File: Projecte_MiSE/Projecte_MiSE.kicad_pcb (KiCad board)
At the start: 2 copper layers, 80 x 75 mm, 36 parts, among them IC1 MSP430FR2355TPT, J1 C_DFrobot, J2 Conn_01x03_Pin, J3 ESP01, J4 URM10, SW1 SW_Push, U1 LMV324, Y1 Crystal_GND3

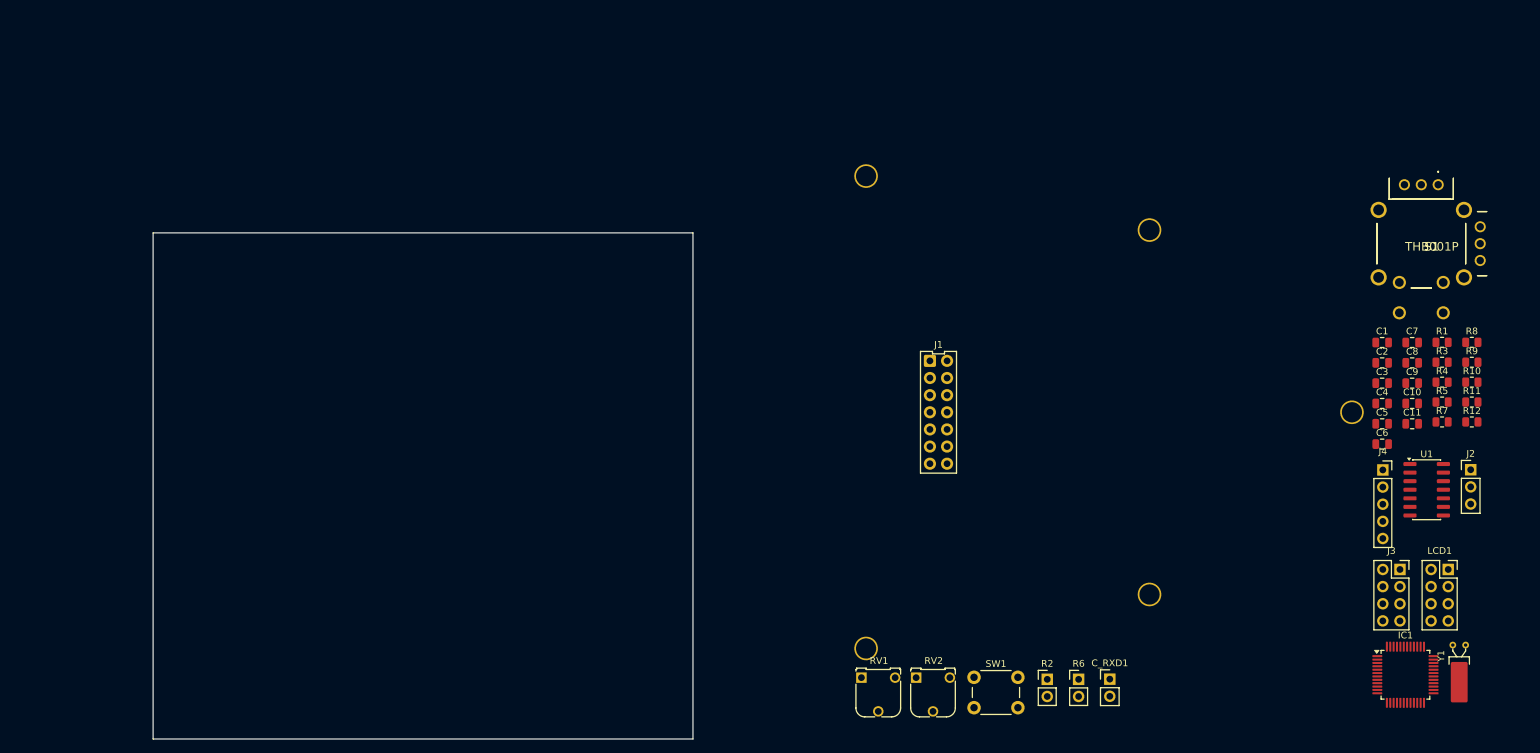
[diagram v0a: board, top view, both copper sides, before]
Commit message: layout LCD i DFrobot
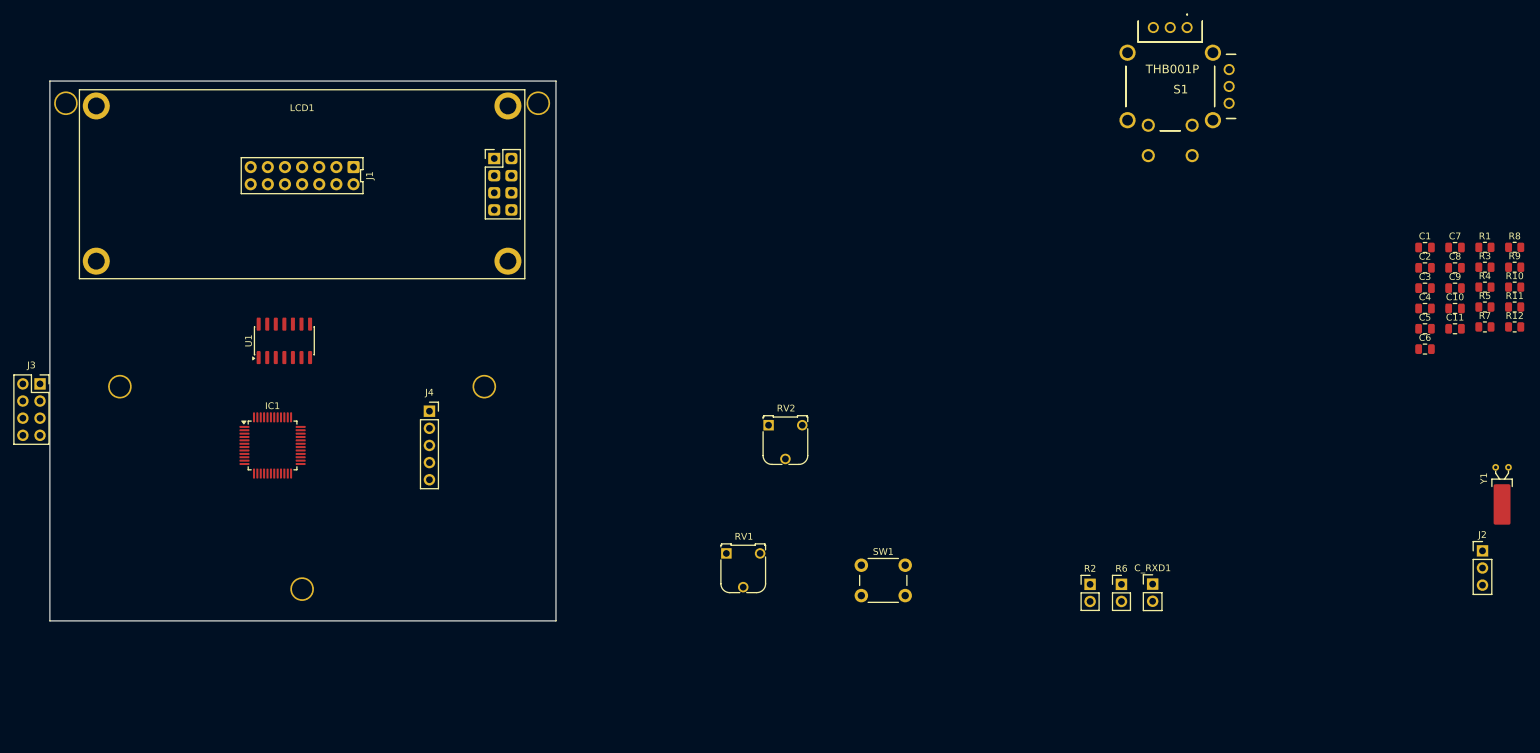
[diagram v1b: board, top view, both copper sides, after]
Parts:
- LCD1: footprint Connector_PinSocket_2.54mm:PinSocket_2x04_P2.54mm_Vertical -> MiSE:LCD_2x16_I2C(Midas)
- moved J3 203.4 mm to (28.8, 77.4)
- moved LCD1 179.2 mm to (67.6, 47.8)
- moved IC1 171.3 mm to (63.2, 86.5)
- moved U1 170.7 mm to (65.0, 71.0), turned to 90 degrees
- moved J4 141.5 mm to (86.5, 81.4)
- moved J1 101.4 mm to (67.6, 47.8), turned to -90 degrees
- moved S1 43.9 mm to (198.8, 24.6)
- moved RV2 43.3 mm to (136.8, 83.5)
- moved RV1 27.2 mm to (130.5, 102.5)
- moved Y1 27.1 mm to (244.5, 89.8)
- moved SW1 23.6 mm to (150.5, 104.2)
- moved C11 15.4 mm to (238.5, 69.2)
- moved C5 15.4 mm to (234.0, 69.2)
- moved R6 15.4 mm to (189.1, 107.1)
- moved C2 15.4 mm to (234.0, 60.2)
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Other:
- board size 80 x 75 mm -> 75 x 80 mm

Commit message: footprints and layout
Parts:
- removed C_RXD1: C_TXD, Connector_PinHeader_2.54mm:PinHeader_1x02_P2.54mm_Vertical
- added D1: LED, LED_SMD:LED_0805_2012Metric, F.Cu at (56.5, 80.2)
- added J10: Conn_GND_TP, Connector_PinHeader_1.00mm:PinHeader_1x01_P1.00mm_Vertical, F.Cu at (73.2, 107.0)
- added J11: Conn_TXD_TP, Connector_PinHeader_1.00mm:PinHeader_1x01_P1.00mm_Vertical, F.Cu at (90.5, 75.2)
- added J12: Conn_RXD_TP, Connector_PinHeader_1.00mm:PinHeader_1x01_P1.00mm_Vertical, F.Cu at (90.5, 69.8)
- added J5: Conn_GND_TP, Connector_PinHeader_1.00mm:PinHeader_1x01_P1.00mm_Vertical, F.Cu at (60.0, 107.0)
- added J6: Conn_ACLK_TP, Connector_PinHeader_1.00mm:PinHeader_1x01_P1.00mm_Vertical, F.Cu at (79.5, 91.5)
- added J7: Conn_SMCLK_TP, Connector_PinHeader_1.00mm:PinHeader_1x01_P1.00mm_Vertical, F.Cu at (79.5, 88.0)
- added J8: Conn_SDA_TP, Connector_PinHeader_1.00mm:PinHeader_1x01_P1.00mm_Vertical, F.Cu at (103.5, 51.5)
- added J9: Conn_SCL_TP, Connector_PinHeader_1.00mm:PinHeader_1x01_P1.00mm_Vertical, F.Cu at (103.5, 43.8)
- added R13: R, Resistor_SMD:R_0805_2012Metric, F.Cu at (53.0, 80.2)
- C1, C2: value C -> 15p
- C3: value C -> 1n
- C4, C5, C6, C7, C8, C9: value C -> 100n
- J2: value Conn_01x03_Pin -> Conn_SWB
- J3: value ESP01 -> ESP01_WIFI
- R3: value R -> 47k
- R4, R5: value R -> 2k2
- R7: value R -> 10k
- SW1: value SW_Push -> ~{RST}
- moved C11 205.4 mm to (33.8, 85.5), turned to 90 degrees
- moved C9 204.6 mm to (34.8, 82.2)
- moved R10 192.9 mm to (56.8, 93.1), turned to 90 degrees
- moved R12 191.2 mm to (58.1, 96.0), turned to 180 degrees
- moved R11 190.3 mm to (59.0, 93.2), turned to -90 degrees
- moved S1 178.0 mm to (33.3, 90.1), turned to 90 degrees
- moved R9 176.5 mm to (73.0, 87.5)
- moved R8 175.9 mm to (74.5, 90.3), turned to -90 degrees
- moved R7 175.0 mm to (67.9, 72.8), turned to 180 degrees
- moved R1 174.1 mm to (72.0, 90.2), turned to 90 degrees
- moved Y1 172.9 mm to (72.0, 78.2), turned to 90 degrees
- moved C10 167.4 mm to (73.2, 93.2)
- moved C2 162.5 mm to (72.0, 73.2), turned to 90 degrees
- moved C5 162.0 mm to (74.3, 42.2), turned to 180 degrees
- moved C4 160.5 mm to (74.3, 50.8), turned to 180 degrees
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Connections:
- net Net-(IC1-P2.1/TB1.2/COMP1.O) renamed /echo
- net Net-(IC1-P4.5/UCB1CLK) renamed /~{RST_{LCD}}
- net Net-(IC1-TEST/SBWTCK) renamed /SBWTCK
- net Net-(IC1-~{RST}/NMI/SBWTDIO) renamed /SBWTDIO
- net Net-(U1A-+) renamed /THR
- net Net-(U1B--) renamed /THL
- net Net-(U1C-+) renamed /THU
- net Net-(U1D--) renamed /THD
- C4 pad 1: Net-(J1-Pin_1) -> +3.3V
- C5 pad 1: Net-(J1-Pin_2) -> +3.3V
- C9 pad 1: Net-(J4-Pin_1) -> +3.3V
- IC1 pad 15: unconnected-(IC1-P4.4/UCB1STE-Pad15) -> /EN
- IC1 pad 17: /EN -> unconnected-(IC1-P6.5/TB3.6-Pad17)
- IC1 pad 2: unconnected-(IC1-P1.1/UCB0CLK/ACLK/OA0O/COMP0.1/A1-Pad2) -> /ACLK_TP
- IC1 pad 3: unconnected-(IC1-P1.0/UCB0STE/SMCLK/COMP0.0/A0/VEREF+-Pad3) -> /SMCLK_TP
- IC1 pad 30: unconnected-(IC1-P2.0/TB1.1/COMP0.O-Pad30) -> /M_L
- J1 pad 1: Net-(J1-Pin_1) -> +3.3V
- J1 pad 2: Net-(J1-Pin_2) -> +3.3V
- J4 pad 1: Net-(J4-Pin_1) -> +3.3V
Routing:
- added copper zone on F.Cu, net +3.3V
- added copper zone on B.Cu, net GND

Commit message: layout and schem pins
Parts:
- moved J11 10.2 mm to (100.2, 78.2)
- moved C8 7.20 mm to (102.0, 63.8), turned to 0 degrees
- moved C5 2.50 mm to (76.8, 42.8), turned to 0 degrees
- moved C4 2.01 mm to (76.2, 50.2), turned to 0 degrees
- moved C6 1.40 mm to (75.7, 80.2)
- moved J6 1.25 mm to (79.5, 92.8)
- moved J7 1.25 mm to (79.5, 89.2)
- moved C2 1.01 mm to (73.0, 73.0)
- moved R11 1.00 mm to (59.0, 92.2)
- moved R12 1.00 mm to (58.1, 95.0)
- moved Y1 1.00 mm to (73.0, 78.2)
- moved R10 0.93 mm to (56.8, 92.2)
- moved R4 0.75 mm to (101.8, 46.7)
- moved R7 0.35 mm to (67.7, 73.0)
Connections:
- IC1 pad 18: /P12 -> /P0
- IC1 pad 19: /P8 -> /P1
- IC1 pad 21: /P1 -> /P8
- IC1 pad 22: /P0 -> /P12
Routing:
- net /SCL: track 0.00 -> 82.1 mm, vias 0 -> 1
- net /SDA: track 0.00 -> 79.8 mm, vias 0 -> 2
- net /TXD: track 0.00 -> 53.1 mm, vias 0 -> 4
- net /RXD: track 0.42 -> 50.9 mm, vias 0 -> 2
- net /LDRR: track 0.00 -> 46.1 mm, vias 0 -> 2
- net /LDRL: track 0.00 -> 45.5 mm, vias 0 -> 2
- net /~{RST_{LCD}}: track 0.00 -> 45.4 mm, vias 0 -> 2
- net /EN: track 0.00 -> 42.3 mm, vias 0 -> 2
- net /SBWTDIO: track 0.00 -> 32.5 mm
- net /P0: track 0.00 -> 30.6 mm
- net /P1: track 0.00 -> 29.7 mm
- net /P2: track 0.00 -> 28.9 mm
- net /trg: track 0.00 -> 28.6 mm
- net /P8: track 0.00 -> 28.0 mm
- net /P12: track 0.00 -> 28.0 mm
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
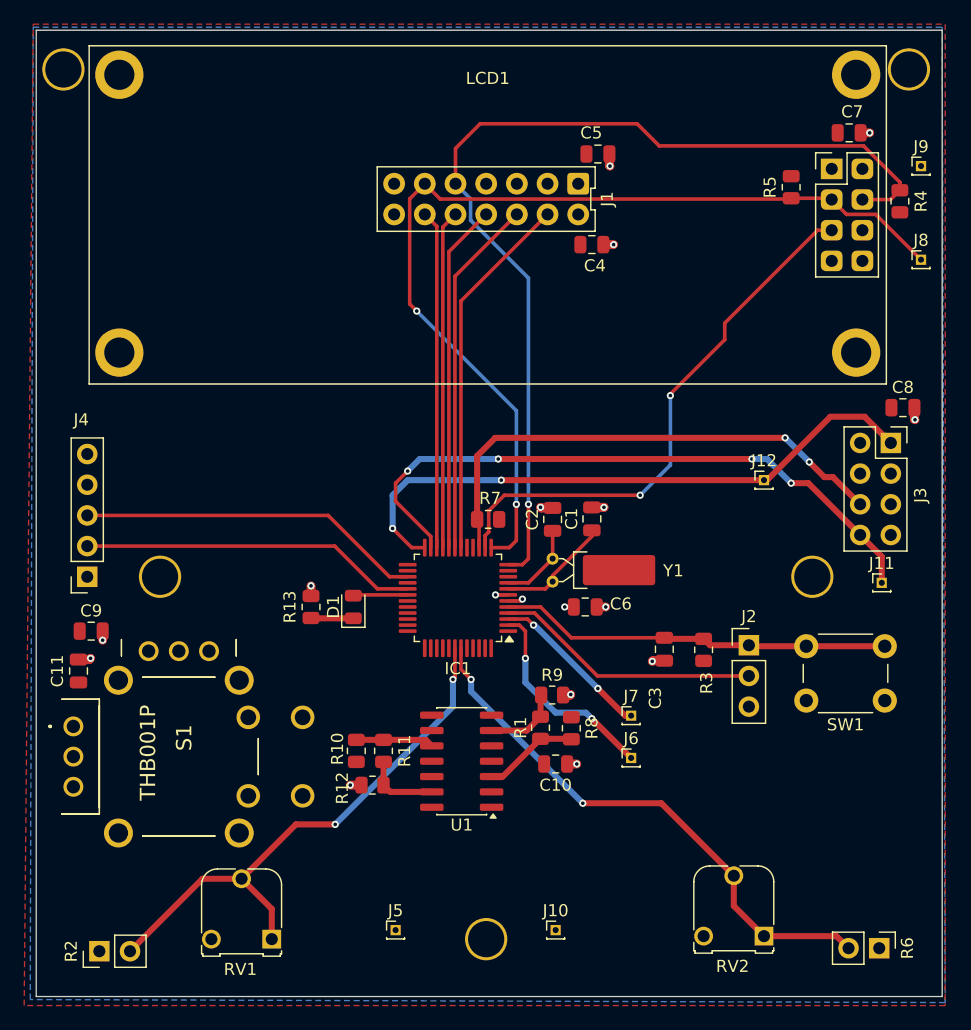
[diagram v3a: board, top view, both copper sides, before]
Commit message: component placement and routing
DRC, constrains and net classes. minor details are missing
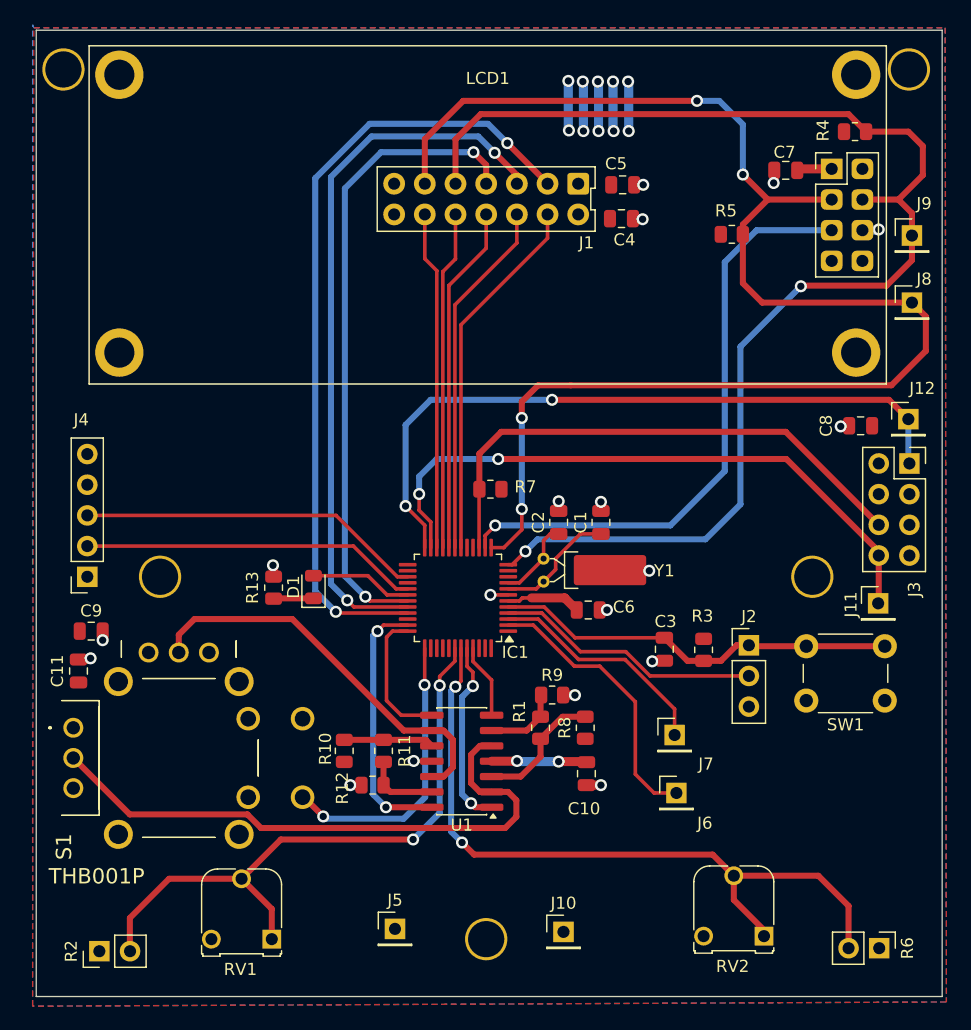
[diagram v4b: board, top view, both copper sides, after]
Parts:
- J10, J11, J12, J5, J6, J7, J8, J9: footprint Connector_PinHeader_1.00mm:PinHeader_1x01_P1.00mm_Vertical -> Connector_PinHeader_2.54mm:PinHeader_1x01_P2.54mm_Vertical
- moved J12 13.0 mm to (102.5, 64.7)
- moved R4 6.85 mm to (98.0, 40.9), turned to 0 degrees
- moved R5 6.27 mm to (87.8, 49.4), turned to 0 degrees
- moved C7 6.10 mm to (92.3, 44.1), turned to 180 degrees
- moved J9 5.80 mm to (102.8, 49.5)
- moved J6 4.74 mm to (83.2, 95.7)
- moved J7 3.94 mm to (83.1, 90.8)
- moved C8 3.81 mm to (98.5, 65.2), turned to 180 degrees
- moved D1 3.69 mm to (53.2, 78.6)
- moved J8 3.63 mm to (102.8, 55.0)
- moved R13 3.49 mm to (49.9, 78.7)
- moved C5 3.27 mm to (78.8, 45.3)
- moved C4 3.26 mm to (78.7, 48.1)
- moved C10 2.67 mm to (75.8, 94.0), turned to -90 degrees
- moved R7 2.51 mm to (67.8, 70.5)
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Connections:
- IC1 pad 35: /GPIOU -> /GPIOD
- IC1 pad 36: /GPIOD -> /GPIOU
- IC1 pad 44: /GPIOL -> /GPIOR
- IC1 pad 45: /GPIOR -> /GPIOL
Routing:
- net /SCLK: track 0.00 -> 65.8 mm, vias 0 -> 2
- net /MISO: track 0.00 -> 59.7 mm, vias 0 -> 2
- net /MOSI: track 0.00 -> 53.1 mm, vias 0 -> 2
- net /ANALOG_OUT1: track 0.00 -> 50.3 mm
- net /SDA: track 79.8 -> 120.5 mm, vias 2 -> 4
- net +3.3V: track 1.99 -> 37.6 mm, vias 2 -> 12
- net /ANALOG_OUT2: track 0.00 -> 33.2 mm
- net /SCL: track 82.1 -> 109.6 mm, vias 1 -> 2
- net /JSEL: track 0.00 -> 24.0 mm, vias 0 -> 2
- net /GPIOD: track 0.00 -> 21.7 mm, vias 0 -> 2
- net /GPIOR: track 0.00 -> 15.6 mm, vias 0 -> 2
- net /LDRL: track 45.5 -> 60.5 mm
- net /GPIOU: track 0.00 -> 11.5 mm
- net /RXD: track 50.9 -> 57.8 mm
- net GND: track 13.5 -> 20.0 mm, vias 15 -> 18
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
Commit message: Crystal
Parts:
- C1, C2: value 15p -> 12p
- R1, R10, R11, R12, R8, R9: value R -> 10k
- R13: value R -> 120
- moved C1 8.28 mm to (76.2, 81.5), turned to 0 degrees
- moved C6 8.27 mm to (70.0, 86.2), turned to -90 degrees
- moved C2 3.59 mm to (76.3, 75.5), turned to 0 degrees
- moved Y1 2.18 mm to (74.0, 79.4)
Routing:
- net /crystall-: track 10.1 -> 8.03 mm
- net +3.3V: track 37.6 -> 39.5 mm, vias 12 -> 14
- net /~{RST_{LCD}}: track 50.3 -> 49.0 mm
- net /SCL: track 109.6 -> 108.5 mm
- net /ANALOG_OUT1: track 50.3 -> 51.2 mm
- net /crystall+: track 6.73 -> 7.57 mm
- net /JSEL: track 24.0 -> 24.6 mm
- net GND: vias 18 -> 17
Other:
- board text added: "Raúl Casado Brandon Ventura MiSE 25/26"

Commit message: Routing correction
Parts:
- added G***: LOGO, MiSE:tux_gnu, F.Cu at (95.2, 96.0)
- moved R10 2.96 mm to (55.2, 89.2), turned to -90 degrees
- moved J11 0.80 mm to (100.8, 80.0)
- moved R7 0.61 mm to (67.5, 70.0)
- moved J6 0.43 mm to (83.0, 96.0)
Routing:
- net /~{RST_{LCD}}: track 49.0 -> 40.8 mm
- net /SCL: track 108.5 -> 101.5 mm
- net /TXD: track 52.4 -> 53.9 mm
- net /THU: track 7.46 -> 8.41 mm
- net /SCLK: track 65.8 -> 66.4 mm
- net /LDRR: track 52.2 -> 52.8 mm
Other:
- board text added: "Raúl Casado Luque K.Brandon Ventura L. MiSE 25/26"
- board text removed: "Raúl Casado Brandon Ventura MiSE 25/26"
